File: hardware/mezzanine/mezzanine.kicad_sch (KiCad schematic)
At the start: 2 parts

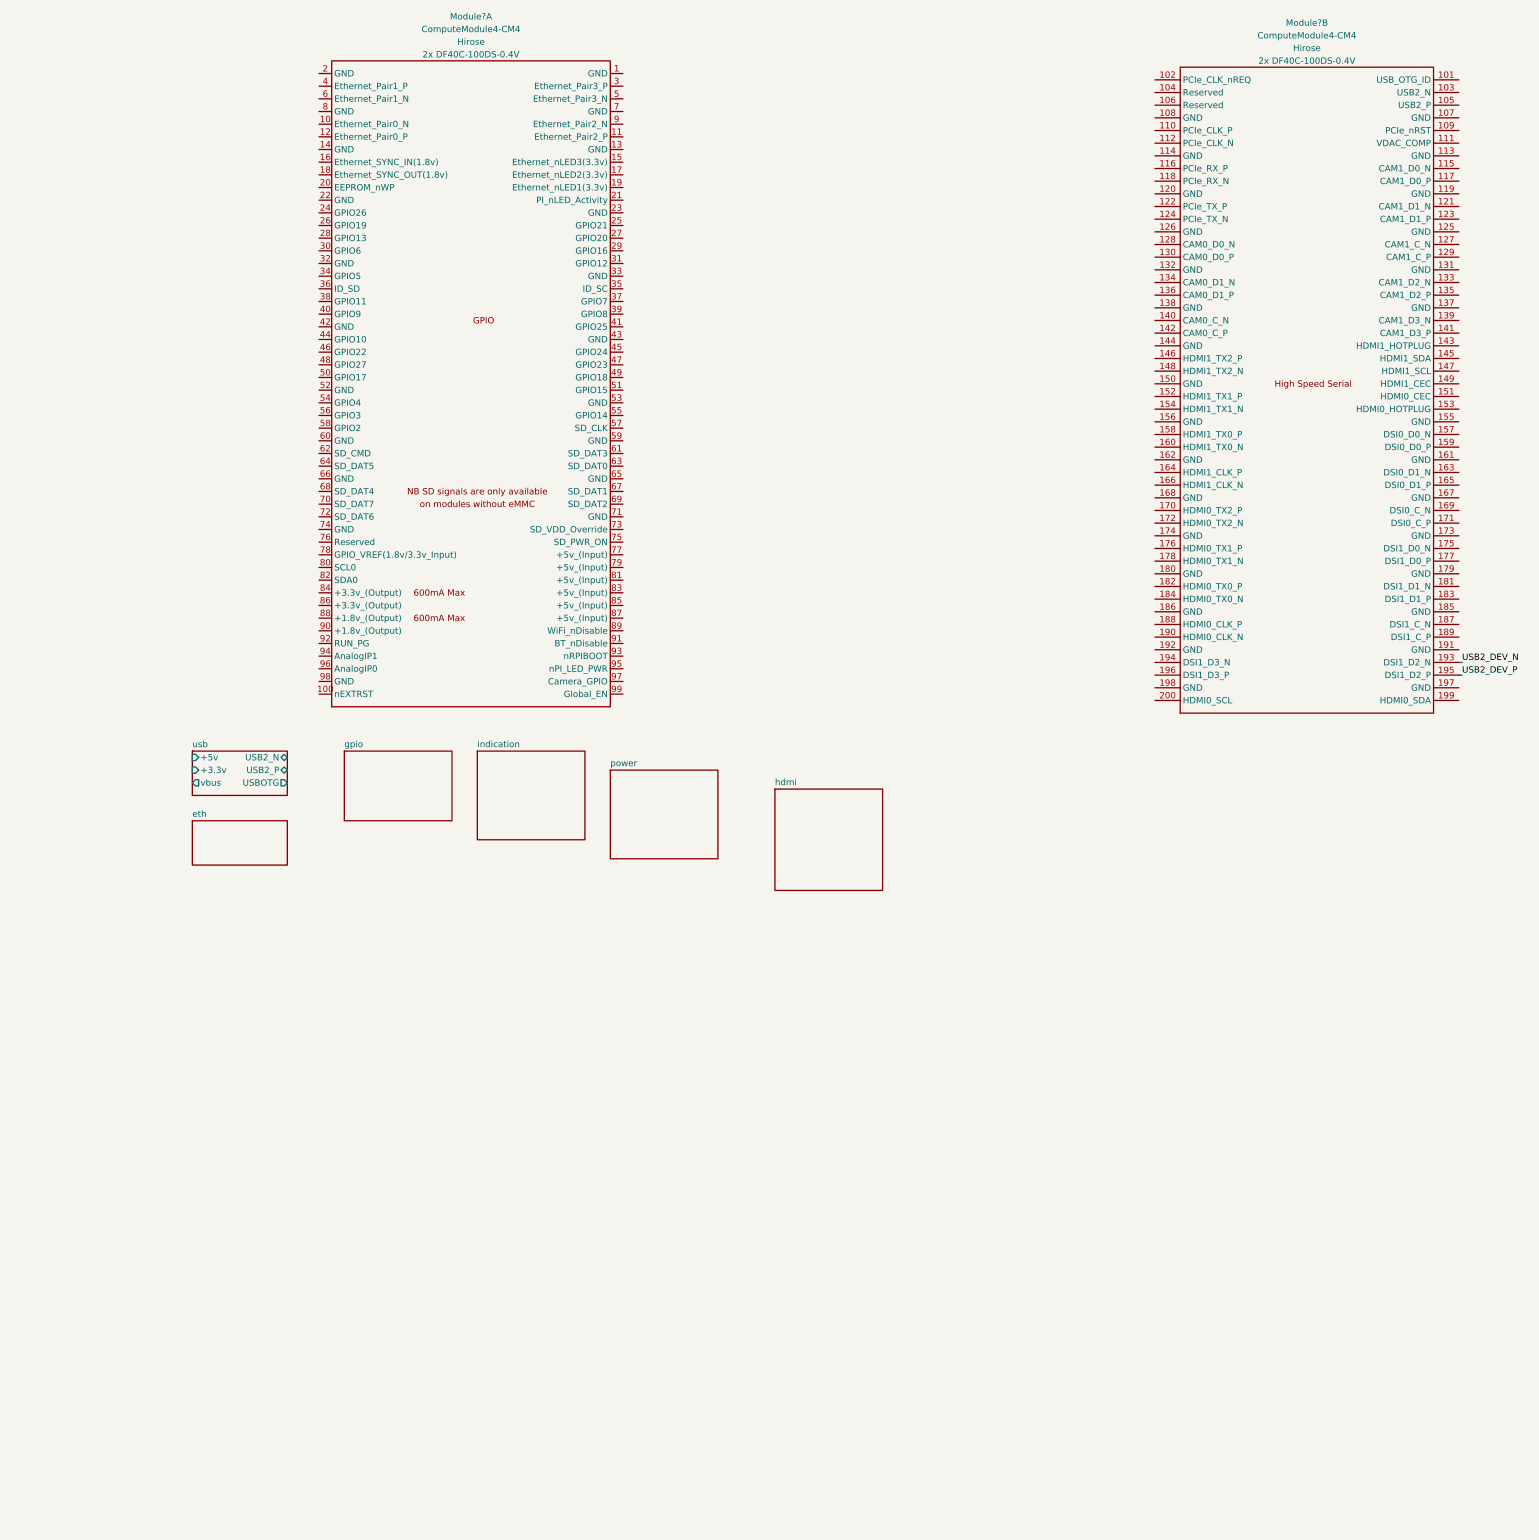
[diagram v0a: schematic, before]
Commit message: start routing mezzanine
making a progress capture before trying to cram a lot of signals onto just one hirose connector...
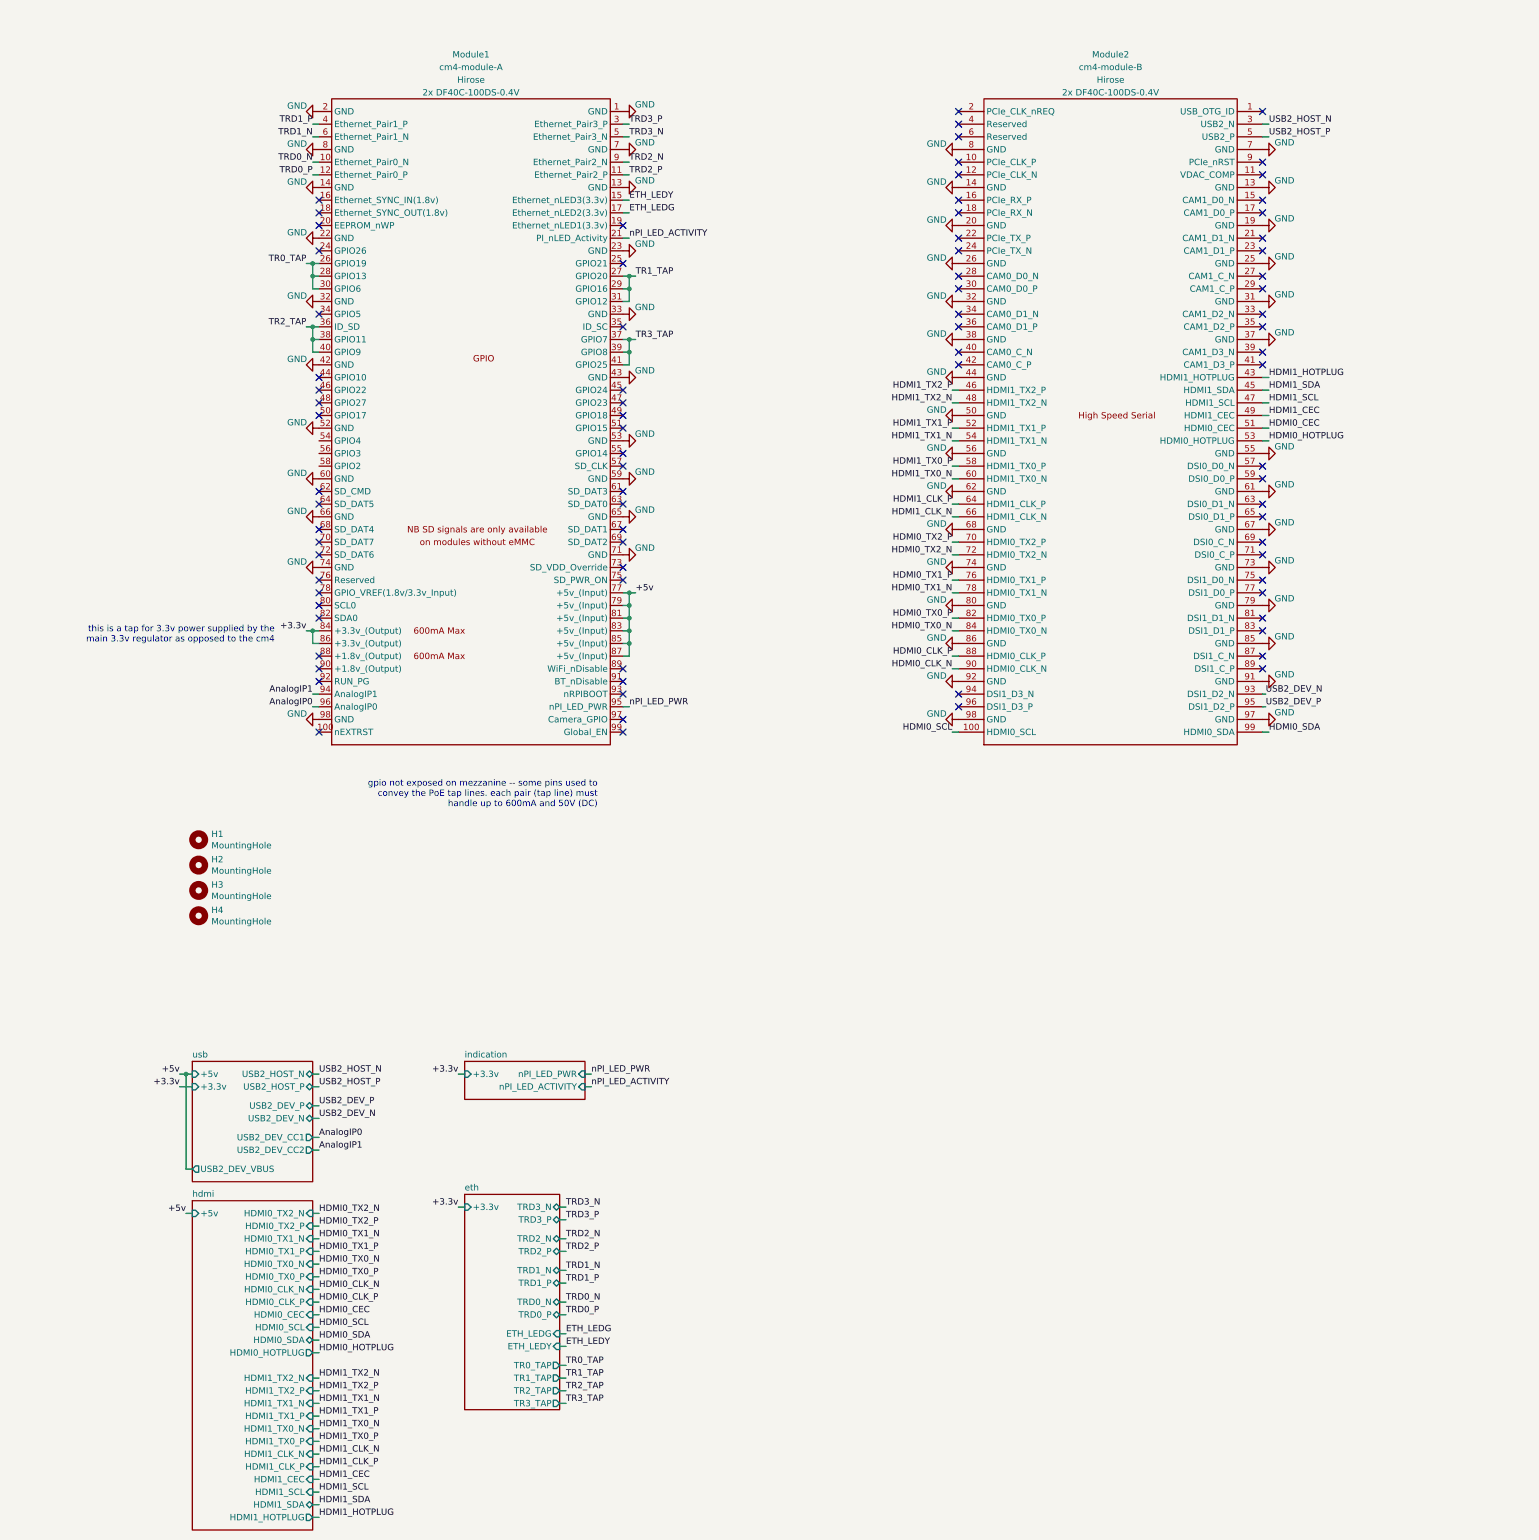
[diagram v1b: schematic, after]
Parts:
- removed Module? (x2): ComputeModule4-CM4, cm4crypto:DF40C-100DP-0.4V(51), symbol cm4crypto:ComputeModule4-CM4
- added H1, H2, H3, H4: MountingHole, MountingHole:MountingHole_2.7mm_M2.5, symbol Mechanical:MountingHole
- added Module1: cm4-module-A, cm4crypto:DF40C-100DP-0.4V(51), symbol cm4crypto:cm4-module-A
- added Module2: cm4-module-B, cm4crypto:DF40C-100DP-0.4V(51), symbol cm4crypto:cm4-module-B
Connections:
- net USB2_DEV_N: now also Module2.93 (DSI1_D2_N)
- net USB2_DEV_P: now also Module2.95 (DSI1_D2_P)
- new net +3.3v: Module1.84 (+3.3v_(Output)), Module1.86 (+3.3v_(Output))
- new net +5v: Module1.77 (+5v_(Input)), Module1.79 (+5v_(Input)), Module1.81 (+5v_(Input)), Module1.83 (+5v_(Input)), Module1.85 (+5v_(Input)), Module1.87 (+5v_(Input))
- new net AnalogIP0: Module1.96 (AnalogIP0)
- new net AnalogIP1: Module1.94 (AnalogIP1)
- new net ETH_LEDG: Module1.17 (Ethernet_nLED2(3.3v))
- new net ETH_LEDY: Module1.15 (Ethernet_nLED3(3.3v))
- new net GND: Module1.1 (GND), Module1.13 (GND), Module1.14 (GND), Module1.2 (GND), Module1.22 (GND), Module1.23 (GND), Module1.32 (GND), Module1.33 (GND), Module1.42 (GND), Module1.43 (GND), Module1.52 (GND), Module1.53 (GND), Module1.59 (GND), Module1.60 (GND), Module1.65 (GND), Module1.66 (GND), Module1.7 (GND), Module1.71 (GND), Module1.74 (GND), Module1.8 (GND), Module1.98 (GND), Module2.13 (GND), Module2.14 (GND), Module2.19 (GND), Module2.20 (GND), Module2.25 (GND), Module2.26 (GND), Module2.31 (GND), Module2.32 (GND), Module2.37 (GND), Module2.38 (GND), Module2.44 (GND), Module2.50 (GND), Module2.55 (GND), Module2.56 (GND), Module2.61 (GND), Module2.62 (GND), Module2.67 (GND), Module2.68 (GND), Module2.7 (GND), Module2.73 (GND), Module2.74 (GND), Module2.79 (GND), Module2.8 (GND), Module2.80 (GND), Module2.85 (GND), Module2.86 (GND), Module2.91 (GND), Module2.92 (GND), Module2.97 (GND), Module2.98 (GND)
- new net HDMI0_CEC: Module2.51 (HDMI0_CEC)
- new net HDMI0_CLK_N: Module2.90 (HDMI0_CLK_N)
- new net HDMI0_CLK_P: Module2.88 (HDMI0_CLK_P)
- new net HDMI0_HOTPLUG: Module2.53 (HDMI0_HOTPLUG)
- new net HDMI0_SCL: Module2.100 (HDMI0_SCL)
- new net HDMI0_SDA: Module2.99 (HDMI0_SDA)
- new net HDMI0_TX0_N: Module2.84 (HDMI0_TX0_N)
- new net HDMI0_TX0_P: Module2.82 (HDMI0_TX0_P)
- new net HDMI0_TX1_N: Module2.78 (HDMI0_TX1_N)
- new net HDMI0_TX1_P: Module2.76 (HDMI0_TX1_P)
- new net HDMI0_TX2_N: Module2.72 (HDMI0_TX2_N)
- new net HDMI0_TX2_P: Module2.70 (HDMI0_TX2_P)
- new net HDMI1_CEC: Module2.49 (HDMI1_CEC)
- new net HDMI1_CLK_N: Module2.66 (HDMI1_CLK_N)
- new net HDMI1_CLK_P: Module2.64 (HDMI1_CLK_P)
- new net HDMI1_HOTPLUG: Module2.43 (HDMI1_HOTPLUG)
- new net HDMI1_SCL: Module2.47 (HDMI1_SCL)
- new net HDMI1_SDA: Module2.45 (HDMI1_SDA)
- new net HDMI1_TX0_N: Module2.60 (HDMI1_TX0_N)
- new net HDMI1_TX0_P: Module2.58 (HDMI1_TX0_P)
- new net HDMI1_TX1_N: Module2.54 (HDMI1_TX1_N)
- new net HDMI1_TX1_P: Module2.52 (HDMI1_TX1_P)
- new net HDMI1_TX2_N: Module2.48 (HDMI1_TX2_N)
- new net HDMI1_TX2_P: Module2.46 (HDMI1_TX2_P)
- new net TR0_TAP: Module1.26 (GPIO19), Module1.28 (GPIO13), Module1.30 (GPIO6)
- new net TR1_TAP: Module1.27 (GPIO20), Module1.29 (GPIO16), Module1.31 (GPIO12)
- new net TR2_TAP: Module1.36 (ID_SD), Module1.38 (GPIO11), Module1.40 (GPIO9)
- new net TR3_TAP: Module1.37 (GPIO7), Module1.39 (GPIO8), Module1.41 (GPIO25)
- new net TRD0_N: Module1.10 (Ethernet_Pair0_N)
- new net TRD0_P: Module1.12 (Ethernet_Pair0_P)
- new net TRD1_N: Module1.6 (Ethernet_Pair1_N)
- new net TRD1_P: Module1.4 (Ethernet_Pair1_P)
- new net TRD2_N: Module1.9 (Ethernet_Pair2_N)
- new net TRD2_P: Module1.11 (Ethernet_Pair2_P)
- new net TRD3_N: Module1.5 (Ethernet_Pair3_N)
- new net TRD3_P: Module1.3 (Ethernet_Pair3_P)
- new net USB2_HOST_N: Module2.3 (USB2_N)
- new net USB2_HOST_P: Module2.5 (USB2_P)
- new net nPI_LED_ACTIVITY: Module1.21 (PI_nLED_Activity)
- new net nPI_LED_PWR: Module1.95 (nPI_LED_PWR)
- no-connect marks 0 -> 84
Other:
- removed sheet gpio
- removed sheet power
- sheet eth ports: added +3.3v, ETH_LEDG, ETH_LEDY, TR0_TAP, TR1_TAP, TR2_TAP, TR3_TAP, TRD0_N, TRD0_P, TRD1_N, TRD1_P, TRD2_N, TRD2_P, TRD3_N, TRD3_P; removed none
- sheet hdmi ports: added +5v, HDMI0_CEC, HDMI0_CLK_N, HDMI0_CLK_P, HDMI0_HOTPLUG, HDMI0_SCL, HDMI0_SDA, HDMI0_TX0_N, HDMI0_TX0_P, HDMI0_TX1_N, HDMI0_TX1_P, HDMI0_TX2_N, HDMI0_TX2_P, HDMI1_CEC, HDMI1_CLK_N, HDMI1_CLK_P, HDMI1_HOTPLUG, HDMI1_SCL, HDMI1_SDA, HDMI1_TX0_N, HDMI1_TX0_P, HDMI1_TX1_N, HDMI1_TX1_P, HDMI1_TX2_N, HDMI1_TX2_P; removed none
- sheet indication ports: added +3.3v, nPI_LED_ACTIVITY, nPI_LED_PWR; removed none
- sheet usb ports: added USB2_DEV_CC1, USB2_DEV_CC2, USB2_DEV_N, USB2_DEV_P, USB2_DEV_VBUS, USB2_HOST_N, USB2_HOST_P; removed USB2_N, USB2_P, USBOTG, vbus
- note added: "gpio not exposed on mezzanine -- some pins used to convey the PoE tap lines. each pair (tap line) must handle up to 600mA and 50V (DC)"
- note added: "this is a tap for 3.3v power supplied by the main 3.3v regulator as opposed to the cm4"

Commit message: finished mezzanine signal routing
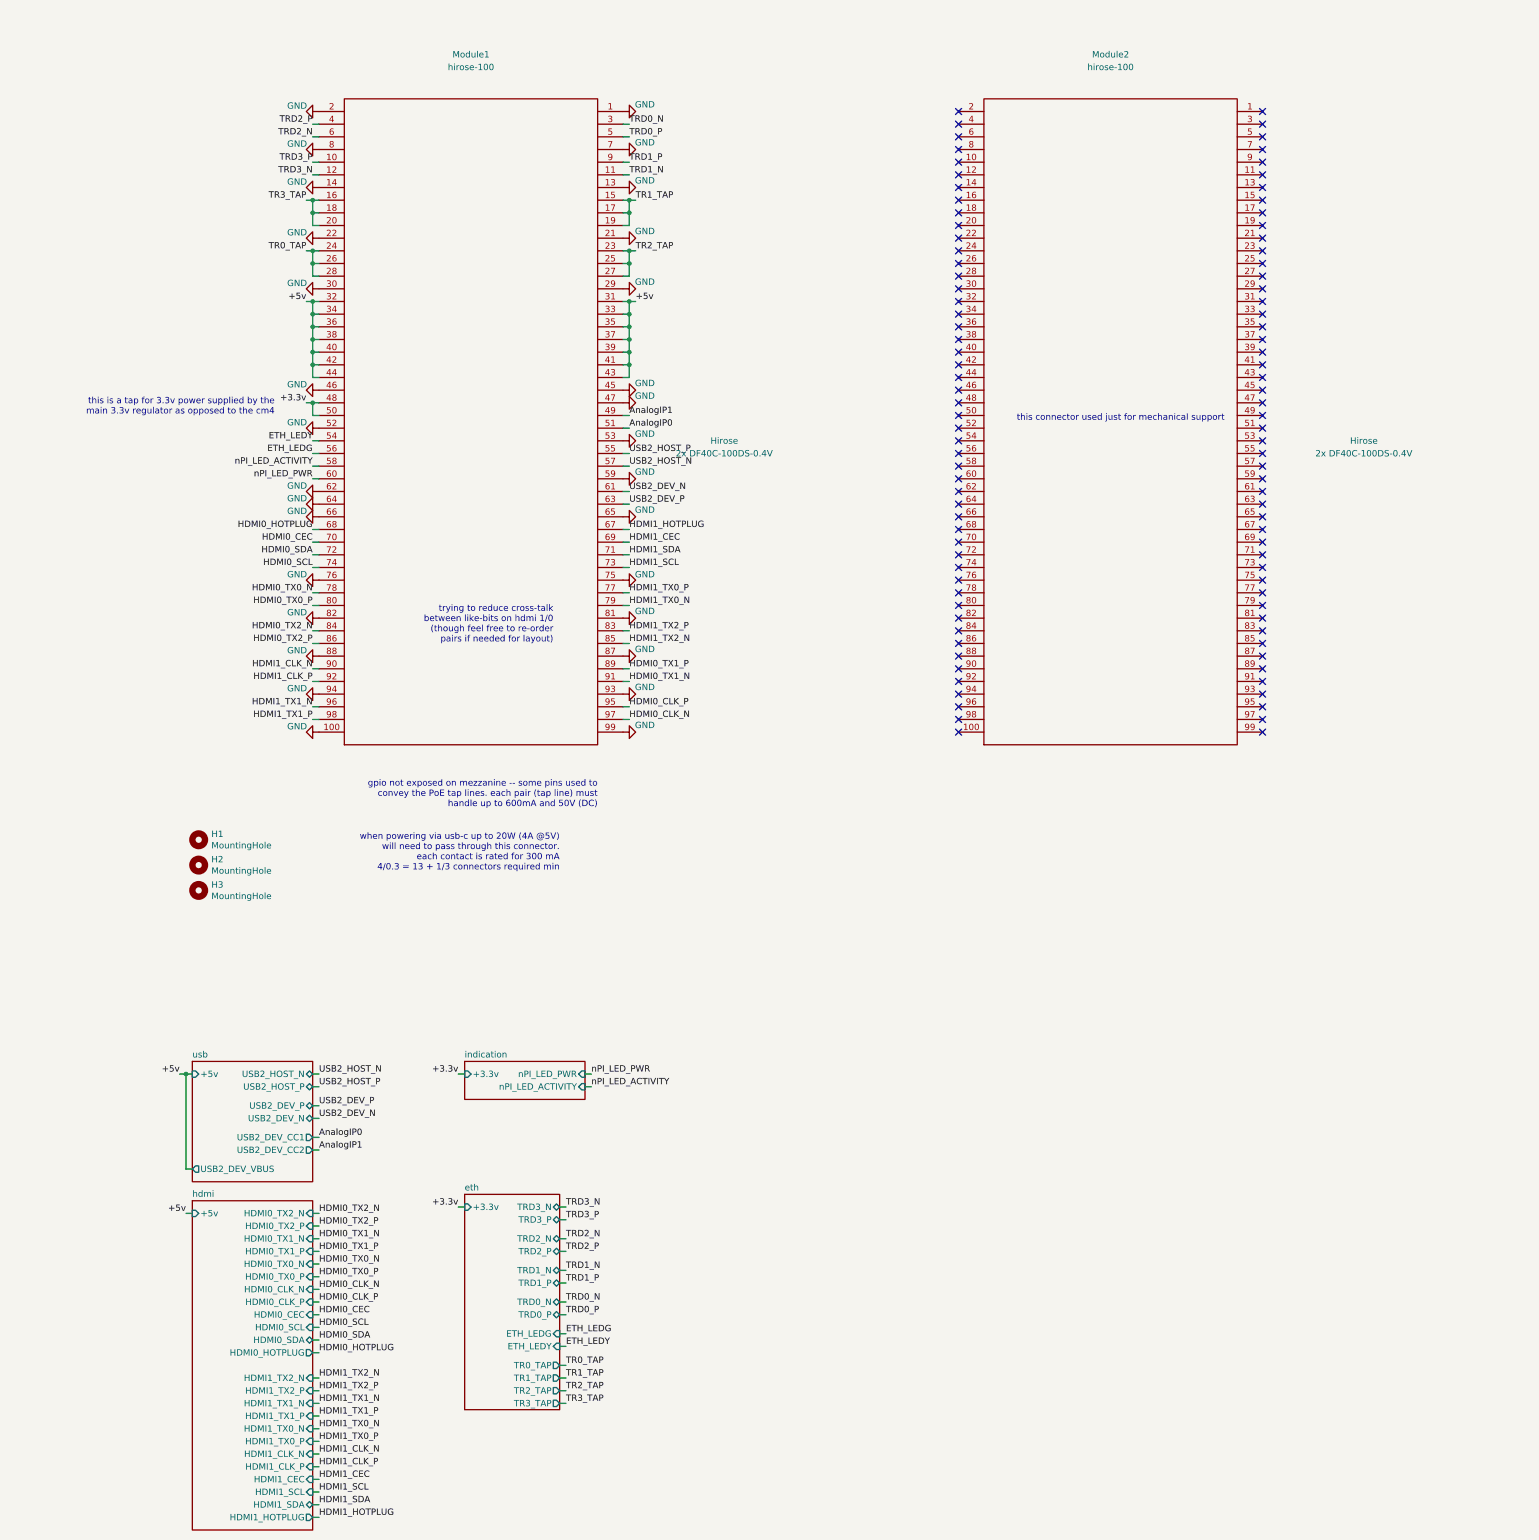
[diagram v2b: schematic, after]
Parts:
- removed H4: MountingHole, MountingHole:MountingHole_2.7mm_M2.5, symbol Mechanical:MountingHole
- removed Module1: cm4-module-A, cm4crypto:DF40C-100DP-0.4V(51), symbol cm4crypto:cm4-module-A
- removed Module2: cm4-module-B, cm4crypto:DF40C-100DP-0.4V(51), symbol cm4crypto:cm4-module-B
- added Module1, Module2: hirose-100, cm4crypto:DF40C-100DP-0.4V(51), symbol cm4crypto:hirose-100
- H1, H2, H3: Field4 nf -> (none); Field5 nf -> (none); Field6 nf -> (none); Field7 nf -> (none); Part Description M2.5 mounting hole -> (none)
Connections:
- net +3.3v: now also Module1.48, Module1.50
- net +5v: now also Module1.31, Module1.32, Module1.33, Module1.34, Module1.35, Module1.36, Module1.37, Module1.38, Module1.39, Module1.40, Module1.41, Module1.42, Module1.43, Module1.44
- net AnalogIP0: now also Module1.51
- net AnalogIP1: now also Module1.49
- net ETH_LEDG: now also Module1.56
- net ETH_LEDY: now also Module1.54
- net GND: now also Module1.1, Module1.100, Module1.13, Module1.14, Module1.2, Module1.21, Module1.22, Module1.29, Module1.30, Module1.45, Module1.46, Module1.47, Module1.52, Module1.53, Module1.59, Module1.62, Module1.64, Module1.65, Module1.66, Module1.7, Module1.75, Module1.76, Module1.8, Module1.81, Module1.82, Module1.87, Module1.88, Module1.93, Module1.94, Module1.99
- net HDMI0_CEC: now also Module1.70
- net HDMI0_CLK_N: now also Module1.97
- net HDMI0_CLK_P: now also Module1.95
- net HDMI0_HOTPLUG: now also Module1.68
- net HDMI0_SCL: now also Module1.74
- net HDMI0_SDA: now also Module1.72
- net HDMI0_TX0_N: now also Module1.78
- net HDMI0_TX0_P: now also Module1.80
- net HDMI0_TX1_N: now also Module1.91
- net HDMI0_TX1_P: now also Module1.89
- net HDMI0_TX2_N: now also Module1.84
- net HDMI0_TX2_P: now also Module1.86
- net HDMI1_CEC: now also Module1.69
- net HDMI1_CLK_N: now also Module1.90
- net HDMI1_CLK_P: now also Module1.92
- net HDMI1_HOTPLUG: now also Module1.67
- net HDMI1_SCL: now also Module1.73
- net HDMI1_SDA: now also Module1.71
- net HDMI1_TX0_N: now also Module1.79
- net HDMI1_TX0_P: now also Module1.77
- net HDMI1_TX1_N: now also Module1.96
- net HDMI1_TX1_P: now also Module1.98
- net HDMI1_TX2_N: now also Module1.85
- net HDMI1_TX2_P: now also Module1.83
- net TR0_TAP: now also Module1.24, Module1.26, Module1.28
- net TR1_TAP: now also Module1.15, Module1.17, Module1.19
- net TR2_TAP: now also Module1.23, Module1.25, Module1.27
- net TR3_TAP: now also Module1.16, Module1.18, Module1.20
- net TRD0_N: now also Module1.3
- net TRD0_P: now also Module1.5
- net TRD1_N: now also Module1.11
- net TRD1_P: now also Module1.9
- net TRD2_N: now also Module1.6
- net TRD2_P: now also Module1.4
- net TRD3_N: now also Module1.12
- net TRD3_P: now also Module1.10
- net USB2_DEV_N: now also Module1.61
- net USB2_DEV_P: now also Module1.63
- net USB2_HOST_N: now also Module1.57
- net USB2_HOST_P: now also Module1.55
- net nPI_LED_ACTIVITY: now also Module1.58
- net nPI_LED_PWR: now also Module1.60
- no-connect marks 84 -> 100
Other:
- sheet usb ports: added none; removed +3.3v
- note added: "this connector used just for mechanical support"
- note added: "trying to reduce cross-talk between like-bits on hdmi 1/0 (though feel free to re-order pairs if needed for layout)"
- note added: "when powering via usb-c up to 20W (4A @5V) will need to pass through this connector. each contact is rated for 300 mA 4/0.3 = 13 + 1/3 connectors required min"

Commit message: sheet refs relative, copied escalator pinout to lobby
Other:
- sheet eth: file C:\Users\Lyocek\Desktop\Tmp\cm4crypto\hardware\mezzanine\sheets\eth.kicad_sch -> ./sheets/eth.kicad_sch
- sheet hdmi: file C:\Users\Lyocek\Desktop\Tmp\cm4crypto\hardware\mezzanine\sheets\hdmi.kicad_sch -> ./sheets/hdmi.kicad_sch
- sheet indication: file C:\Users\Lyocek\Desktop\Tmp\cm4crypto\hardware\mezzanine\sheets\indication.kicad_sch -> ./sheets/indication.kicad_sch
- sheet usb: file C:\Users\Lyocek\Desktop\Tmp\cm4crypto\hardware\mezzanine\sheets\usb.kicad_sch -> ./sheets/usb.kicad_sch
